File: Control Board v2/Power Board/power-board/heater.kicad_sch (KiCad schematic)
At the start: 12 parts, among them J2 1366005, U2 MOC3083S-TA1

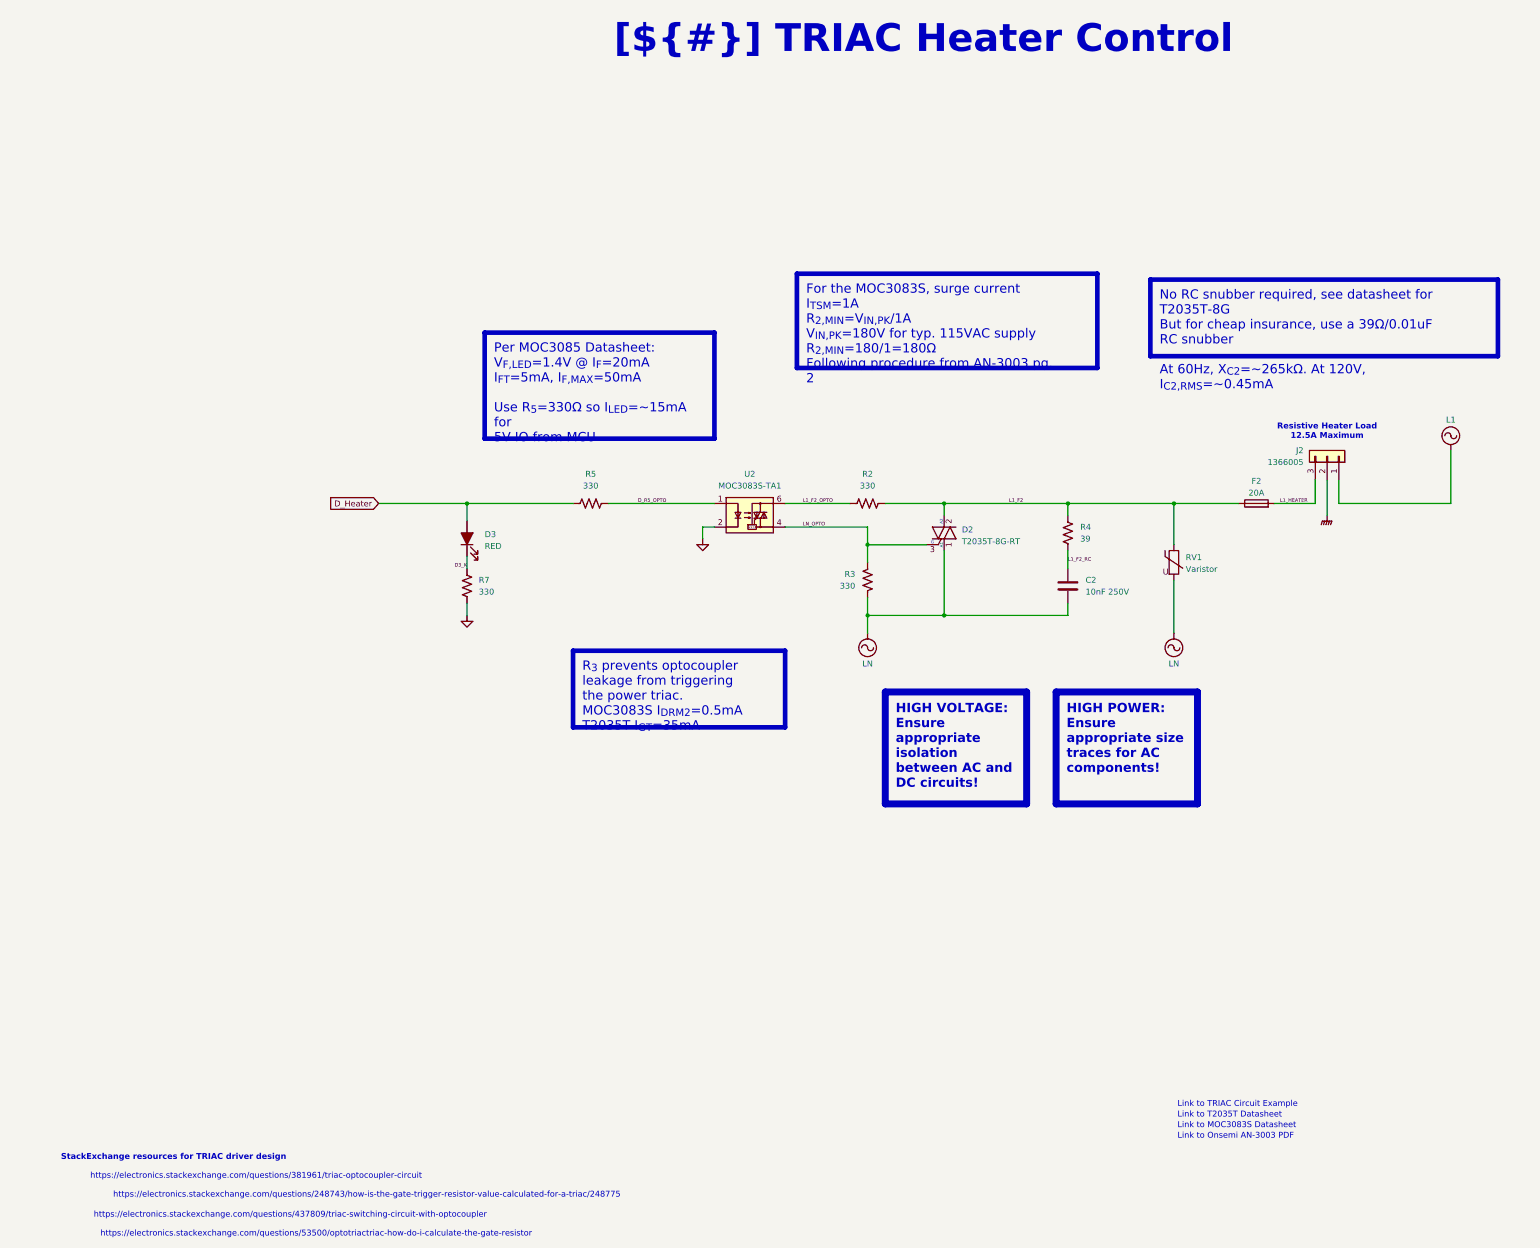
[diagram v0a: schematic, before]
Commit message: schematic mostly done, start board layout
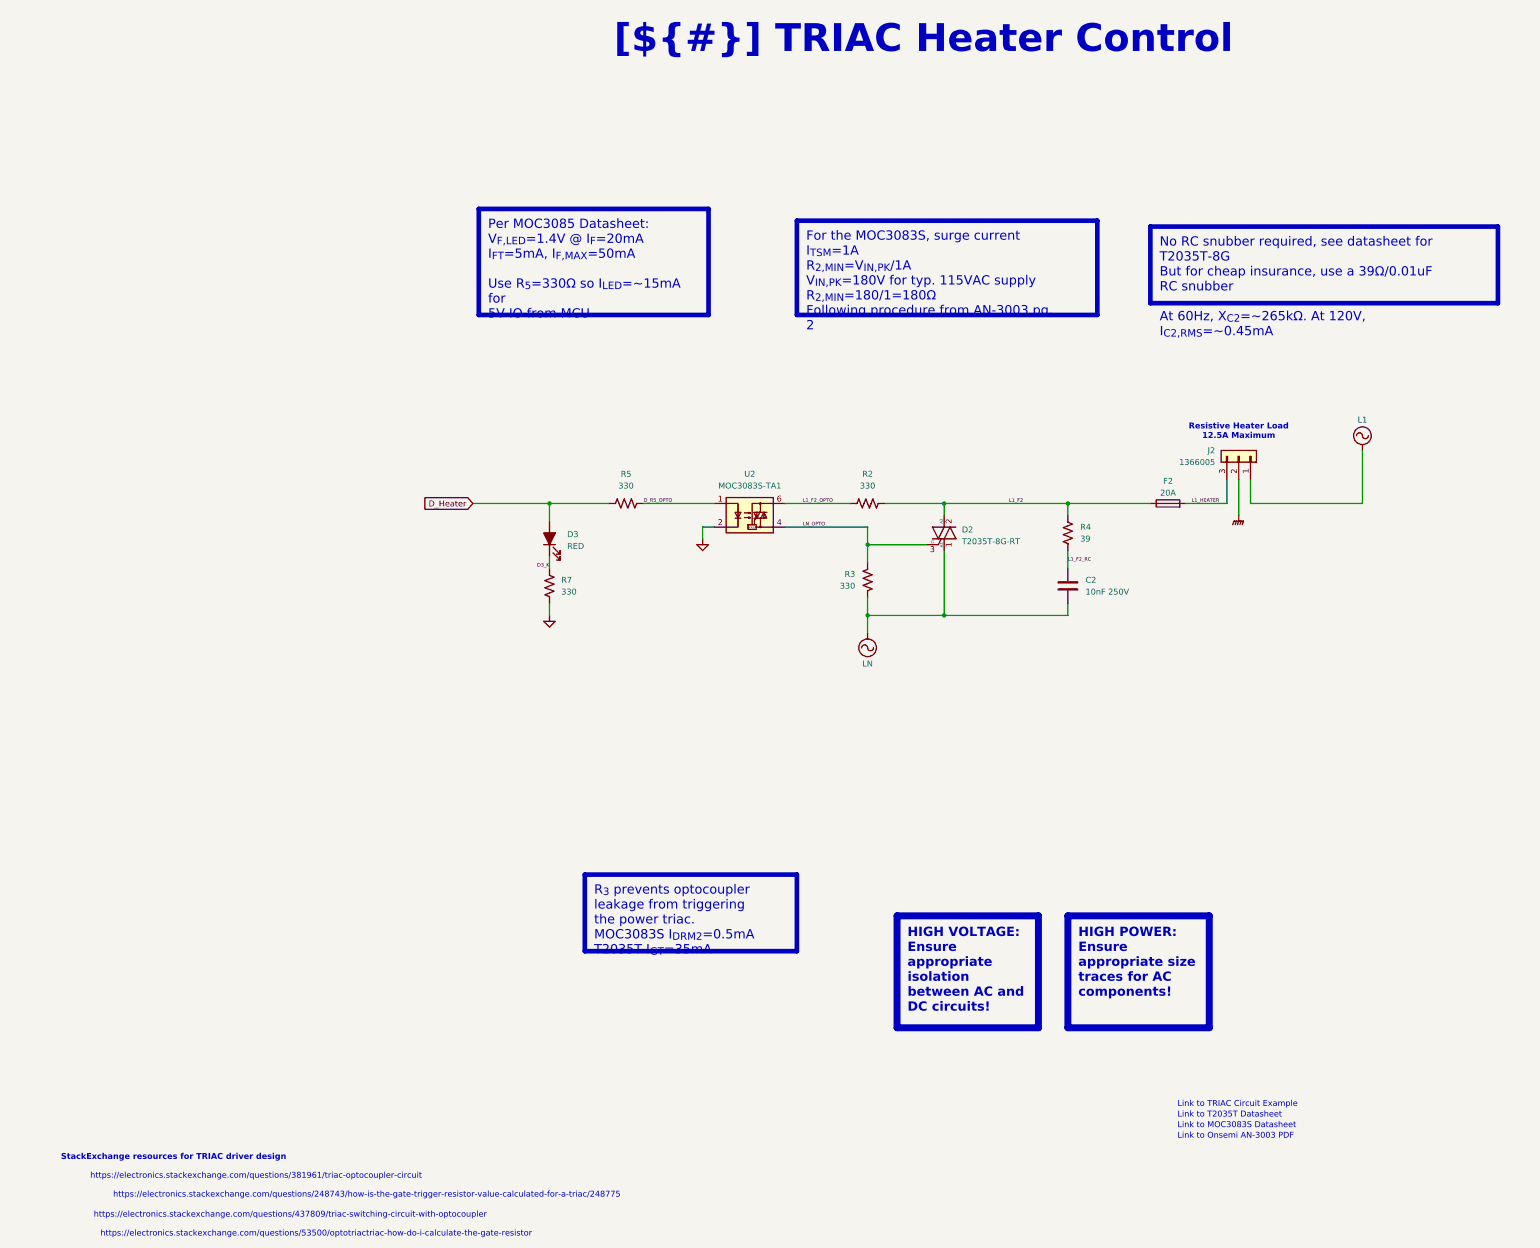
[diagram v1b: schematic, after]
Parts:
- removed RV1: Varistor, symbol Device:Varistor
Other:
- moved on the sheet: D3, F2, J2, R5, R7

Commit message: PCB layout is generally complete
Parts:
- added J3: Conn_01x03, Connector_PinHeader_2.54mm:PinHeader_1x03_P2.54mm_Vertical, symbol Connector_Generic:Conn_01x03
- C2: footprint Capacitor_SMD:C_1206_3216Metric_Pad1.33x1.80mm_HandSolder -> Capacitor_SMD:C_1812_4532Metric_Pad1.57x3.40mm_HandSolder
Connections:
- net D_Heater: now also J3.2 (Pin_2)
- net GND: now also J3.1 (Pin_1)
- new net VDD: J3.3 (Pin_3)
